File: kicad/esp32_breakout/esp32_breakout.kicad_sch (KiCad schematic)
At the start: 26 parts, among them J1 JST B5B-PH-K-S, J10 JST B6B-PH-K-S, J2 JST B5B-PH-K-S, J3 JST B7B-PH-K-S, J4 XT30U-M, J5 HDR F 2.54MM VERT, J6 HDR F 2.54MM 5-pin VERT, J9 JST B6B-PH-K-S, SW1 SS12D10, U1 ESP32 DEV KIT Module 30-pin, U2 LM2596 Module

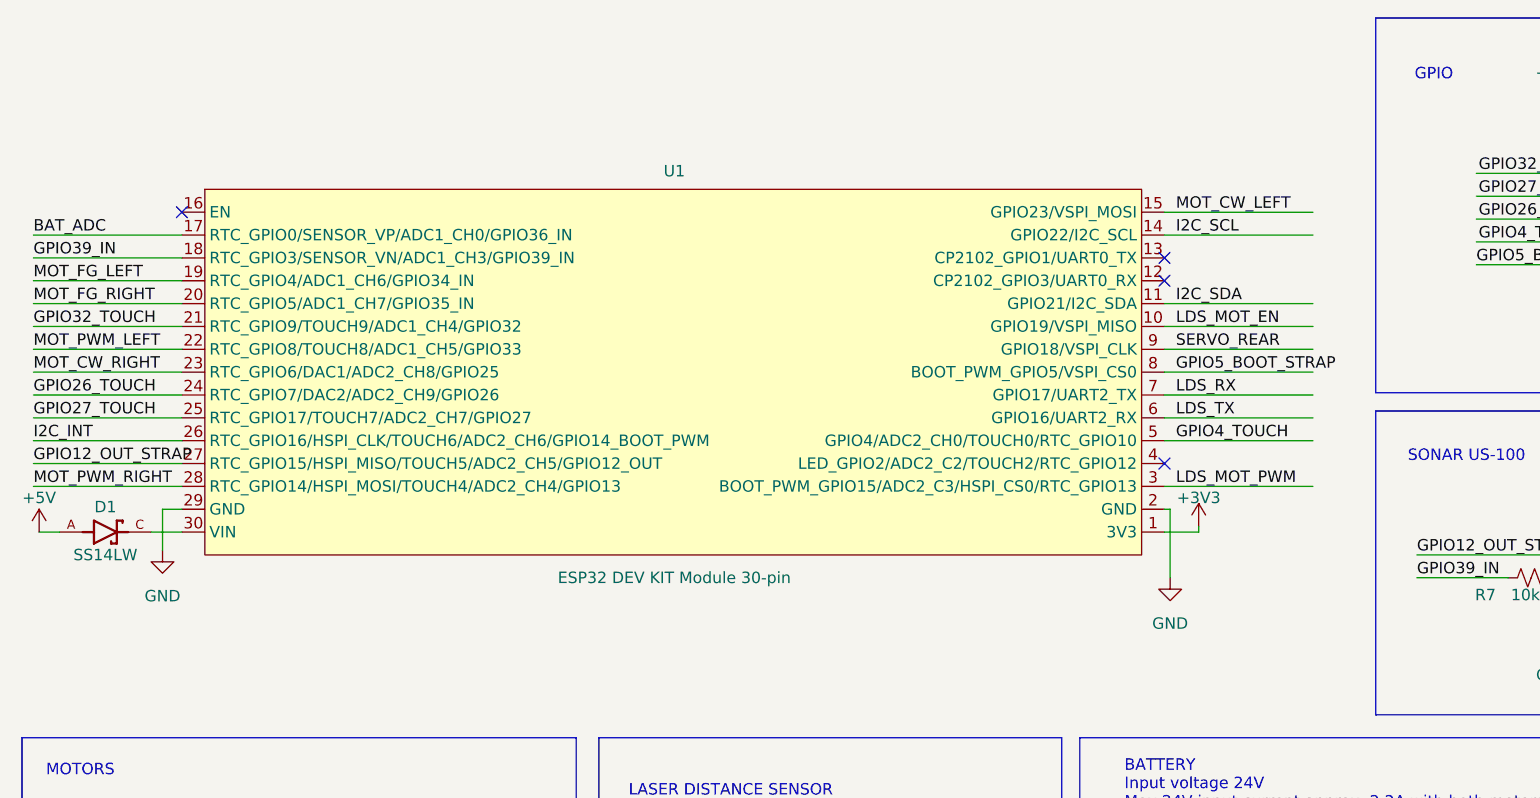
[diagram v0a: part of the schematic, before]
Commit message: Pico head breakout layout start
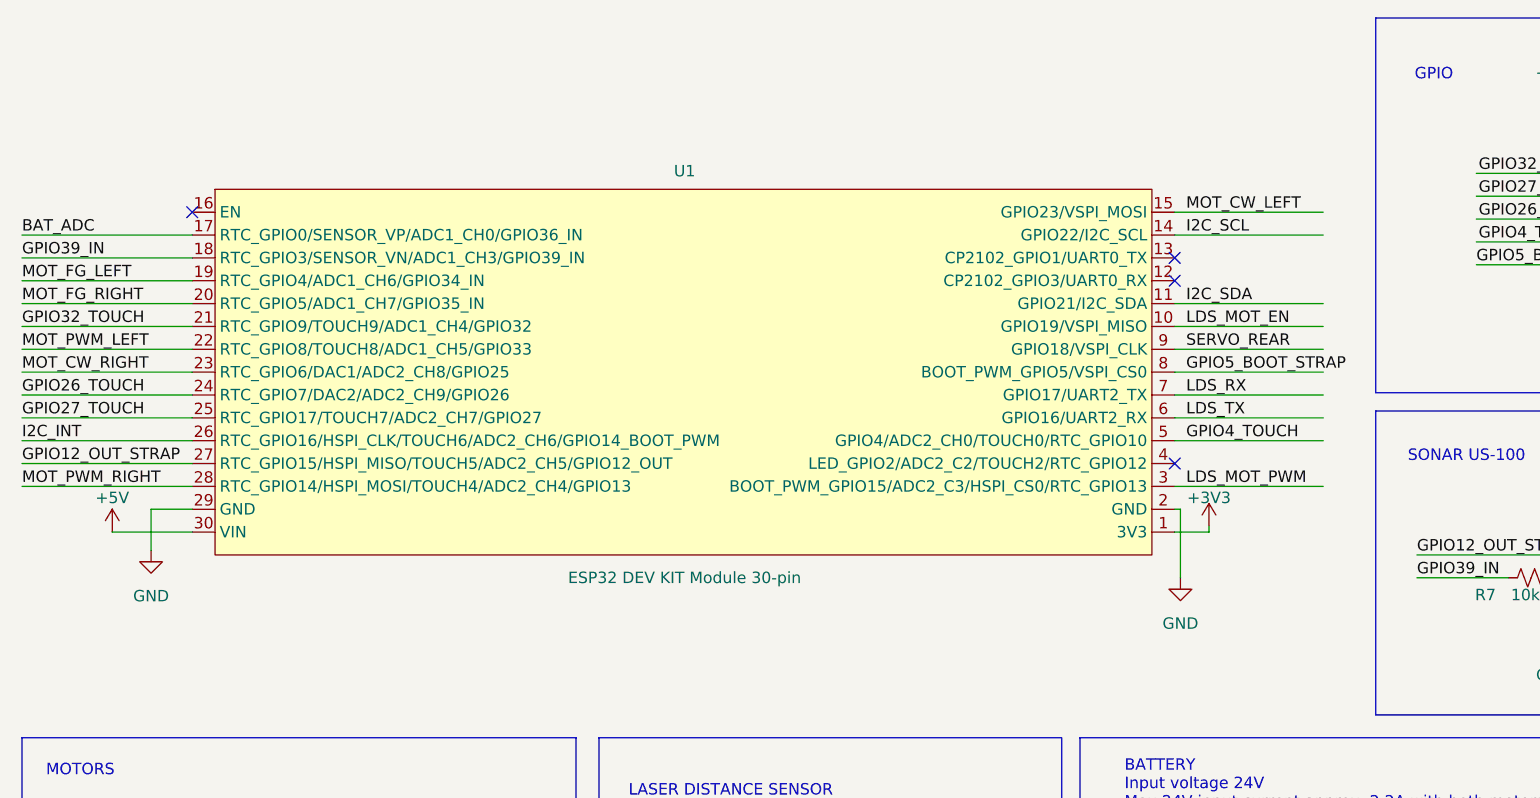
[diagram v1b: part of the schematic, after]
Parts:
- removed D1: SS14LW, SS14LW:DIO_SS14LW, symbol Makerspet:SS14LW
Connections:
- net +5V: now also U1.30 (VIN)
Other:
- moved on the sheet: U1

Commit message: ESP32 breakout v1.0
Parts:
- added D1: FS26, Diode_SMD:D_SOD-123F, symbol Device:D_Schottky
- J4: footprint Connector_AMASS:AMASS_XT30U-M_1x02_P5.0mm_Vertical -> Makerspet:AMASS_XT30U-F_1x02_P5.0mm_Vertical
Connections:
- net +5V: now also D1.2 (A); no longer U1.30 (VIN)
- new net: D1.1 (K), U1.30 (VIN)
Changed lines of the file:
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@@
   (title_block
     (title "Maker's Pet ESP32 Breakout")
-    (date "2023-12-12")
+    (date "2023-12-15")
     (rev "1.0.0")
     (company "Maker's Pet")
@@
     (stroke (width 0) (type default))
   )
+  (wire (pts (xy 27.94 72.39) (xy 33.528 72.39))
+    (stroke (width 0) (type default))
+  )
   (wire (pts (xy 143.383 69.85) (xy 143.383 77.47))
     (stroke (width 0) (type default))
@@
     (stroke (width 0) (type default))
   )
+  (wire (pts (xy 18.034 72.39) (xy 20.32 72.39))
+    (stroke (width 0) (type default))
+  )
   (wire (pts (xy 176.276 40.132) (xy 194.056 40.132))
     (stroke (width 0) (type default))
@@
   )
   (wire (pts (xy 146.05 150.114) (xy 162.56 150.114))
-    (stroke (width 0) (type default))
-  )
-  (wire (pts (xy 24.638 72.39) (xy 33.528 72.39))
     (stroke (width 0) (type default))
   )
@@
     )
   )
+  (symbol (lib_id "Device:D_Schottky") (at 24.13 72.39 0) (mirror y) (unit 1)
+    (in_bom yes) (on_board yes) (dnp no)
+    (property "Reference" "D1" (at 24.13 69.342 0)
+      (effects (font (size 1.27 1.27)))
+    )
+    (property "Value" "FS26" (at 23.876 75.438 0)
+      (effects (font (size 1.27 1.27)))
+    )
+    (property "Footprint" "Diode_SMD:D_SOD-123F" (at 24.13 72.39 0)
+      (effects (font (size 1.27 1.27)) hide)
+    )
+    (property "Datasheet" "https://www.digikey.com/en/products/detail/good-ark-semiconductor/FS26/18667798" (at 24.13 72.39 0)
+      (effects (font (size 1.27 1.27)) hide)
+    )
+    (pin "2")
+    (pin "1")
+    (instances
+      (project "esp32_breakout"
+        (path "/e24ae185-8f18-408c-aee8-f727519bade3"
+          (reference "D1") (unit 1)
+        )
+      )
+    )
+  )
   (symbol (lib_id "Switch:SW_SPDT") (at 189.23 127 0) (mirror y) (unit 1)
     (in_bom yes) (on_board yes) (dnp no)
@@
         (path "/e24ae185-8f18-408c-aee8-f727519bade3"
           (reference "H1") (unit 1)
-        )
-      )
-    )
-  )
-  (symbol (lib_id "power:+5V") (at 24.638 72.39 0) (unit 1)
-    (in_bom yes) (on_board yes) (dnp no) (fields_autoplaced)
-    (property "Reference" "#PWR02" (at 24.638 76.2 0)
-      (effects (font (size 1.27 1.27)) hide)
-    )
-    (property "Value" "+5V" (at 24.638 68.58 0)
-      (effects (font (size 1.27 1.27)))
-    )
-    (property "Footprint" "" (at 24.638 72.39 0)
-      (effects (font (size 1.27 1.27)) hide)
-    )
-    (property "Datasheet" "" (at 24.638 72.39 0)
-      (effects (font (size 1.27 1.27)) hide)
-    )
-    (pin "1")
-    (instances
-      (project "esp32_breakout"
-        (path "/e24ae185-8f18-408c-aee8-f727519bade3"
-          (reference "#PWR02") (unit 1)
         )
       )
@@
     )
   )
+  (symbol (lib_id "power:+5V") (at 18.034 72.39 0) (unit 1)
+    (in_bom yes) (on_board yes) (dnp no) (fields_autoplaced)
+    (property "Reference" "#PWR02" (at 18.034 76.2 0)
+      (effects (font (size 1.27 1.27)) hide)
+    )
+    (property "Value" "+5V" (at 18.034 68.58 0)
+      (effects (font (size 1.27 1.27)))
+    )
+    (property "Footprint" "" (at 18.034 72.39 0)
+      (effects (font (size 1.27 1.27)) hide)
+    )
+    (property "Datasheet" "" (at 18.034 72.39 0)
+      (effects (font (size 1.27 1.27)) hide)
+    )
+    (pin "1")
+    (instances
+      (project "esp32_breakout"
+        (path "/e24ae185-8f18-408c-aee8-f727519bade3"
+          (reference "#PWR02") (unit 1)
+        )
+      )
+    )
+  )
   (symbol (lib_id "Device:D_Schottky") (at 177.546 124.46 0) (mirror y) (unit 1)
     (in_bom yes) (on_board yes) (dnp no) (fields_autoplaced)
@@
       (effects (font (size 1.27 1.27)))
     )
-    (property "Footprint" "Connector_AMASS:AMASS_XT30U-M_1x02_P5.0mm_Vertical" (at 147.066 119.38 0)
-      (effects (font (size 1.27 1.27)) hide)
-    )
+    (property "Footprint" "Makerspet:AMASS_XT30U-F_1x02_P5.0mm_Vertical" (at 147.066 119.38 0)
+      (effects (font (size 1.27 1.27)) hide)
+    )

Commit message: Socket header
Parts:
- J6: footprint Connector_PinHeader_2.54mm:PinHeader_1x05_P2.54mm_Vertical -> Connector_PinSocket_2.54mm:PinSocket_1x05_P2.54mm_Vertical
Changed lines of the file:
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@@
       (effects (font (size 1.27 1.27)) (justify left))
     )
-    (property "Footprint" "Connector_PinHeader_2.54mm:PinHeader_1x05_P2.54mm_Vertical" (at 192.532 77.47 0)
+    (property "Footprint" "Connector_PinSocket_2.54mm:PinSocket_1x05_P2.54mm_Vertical" (at 192.532 77.47 0)
       (effects (font (size 1.27 1.27)) hide)
     )

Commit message: ESP32 board v1.1
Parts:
- added D3: FS26, Diode_SMD:D_SOD-123F, symbol Device:D_Schottky
- added Q1: AS2302, Package_TO_SOT_SMD:SOT-23, symbol Transistor_FET:BSS123
- added R5, R6: 10k, Resistor_SMD:R_0603_1608Metric, symbol Device:R_Small_US
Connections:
- net +5V: now also D3.1 (K)
- net GND: now also Q1.2 (S)
- net LDS_MOT_PWM: now also R5.2
- net LDS_TX: now also R6.1; no longer J3.2 (Pin_2)
- net LDS_MOT-: now reaches J3.6 (Pin_6)
- net LDS_MOT-: now also D3.2 (A), Q1.3 (D)
- new net: J3.2 (Pin_2), R6.2
- new net: Q1.1 (G), R5.1
- no-connect marks 6 -> 5

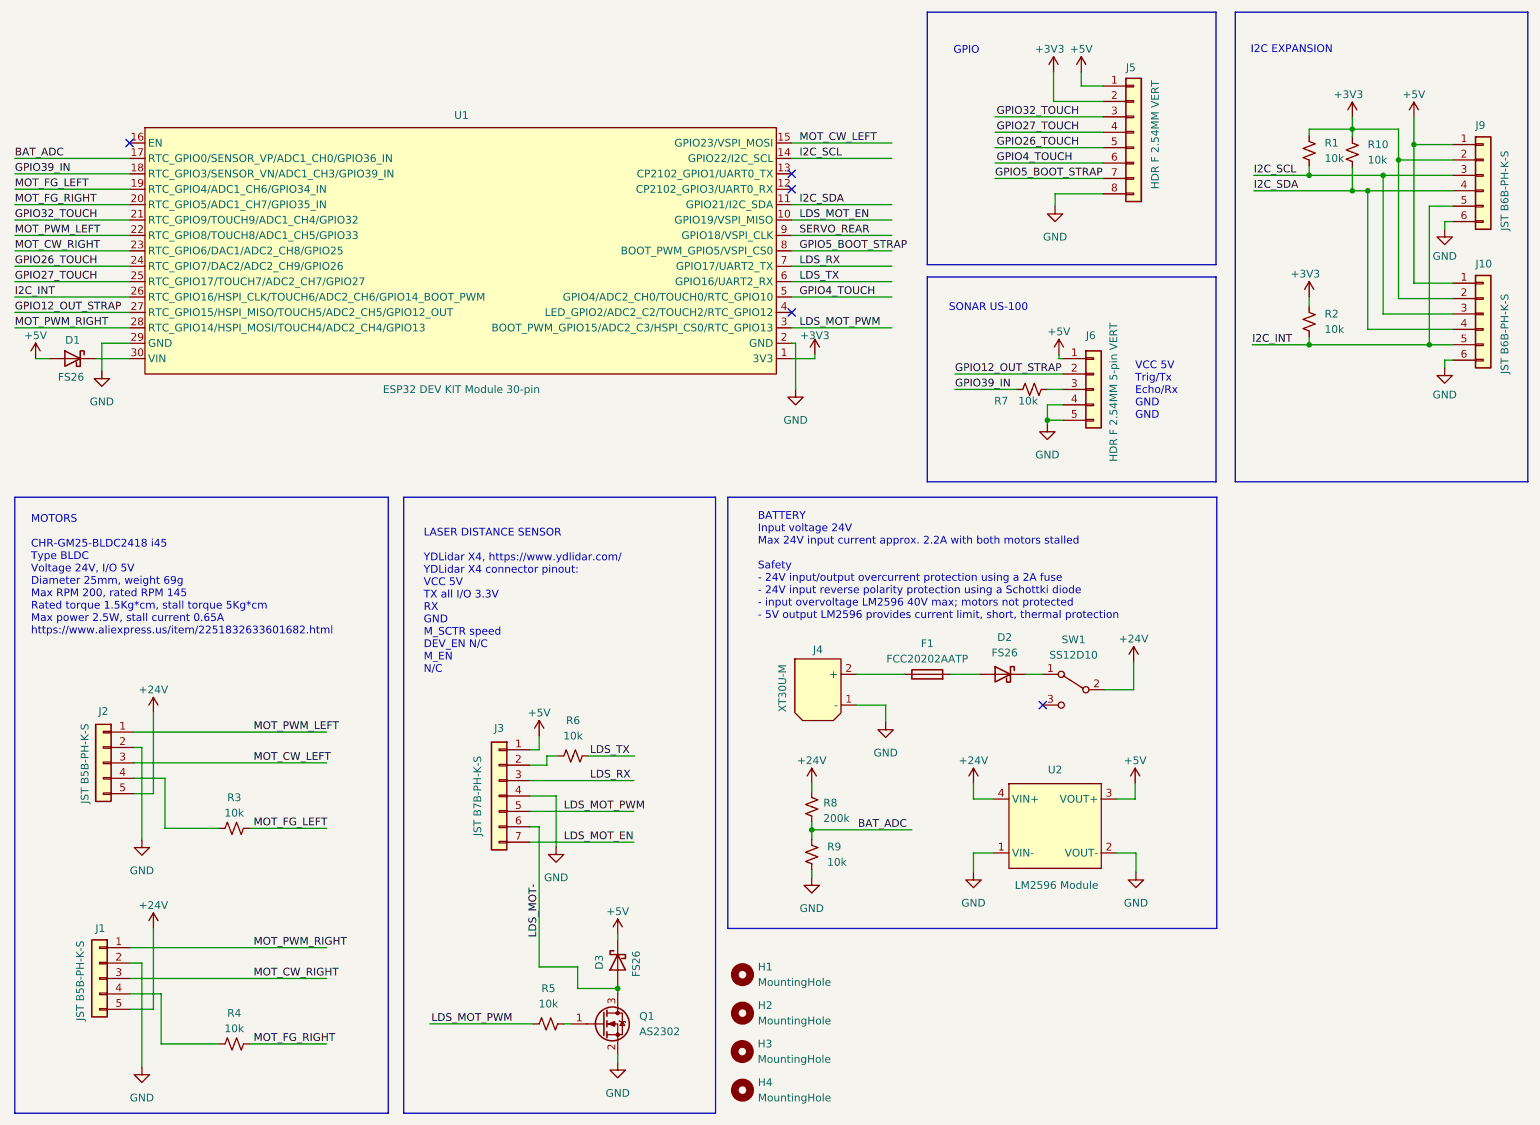
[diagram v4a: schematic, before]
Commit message: Reverted ESP32 PCB to v1
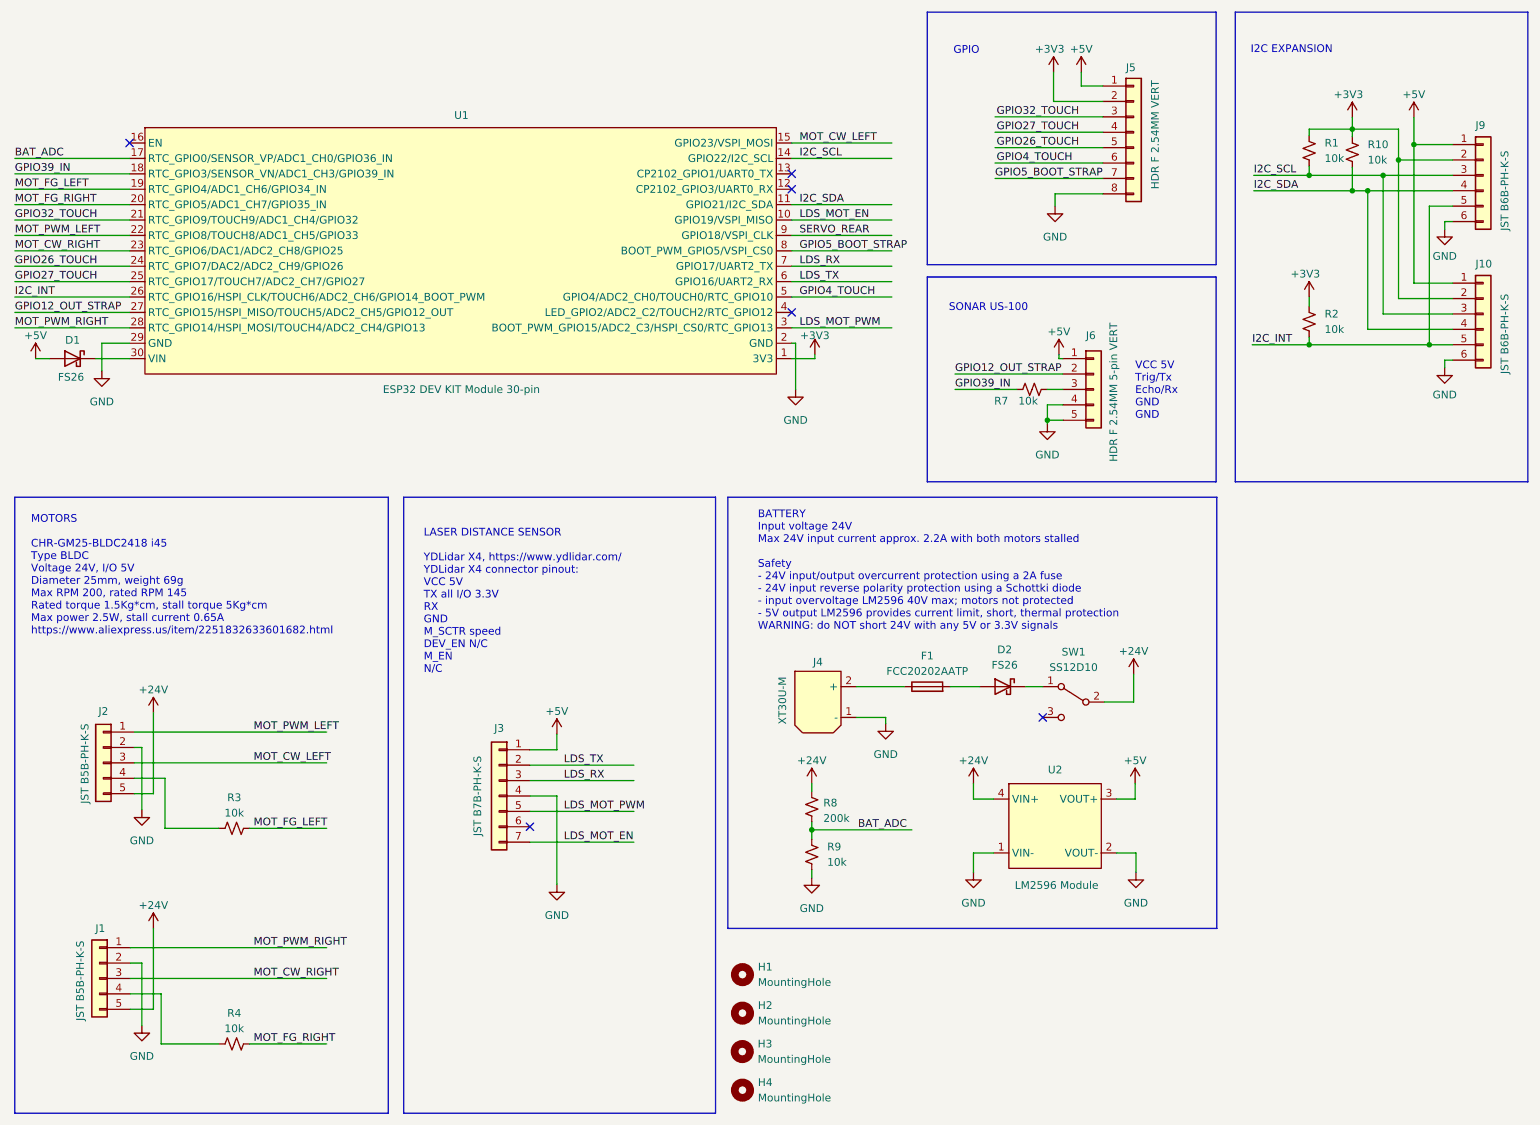
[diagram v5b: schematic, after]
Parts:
- removed D3: FS26, Diode_SMD:D_SOD-123F, symbol Device:D_Schottky
- removed Q1: AS2302, Package_TO_SOT_SMD:SOT-23, symbol Transistor_FET:BSS123
- removed R5, R6: 10k, Resistor_SMD:R_0603_1608Metric, symbol Device:R_Small_US
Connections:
- net LDS_TX: now also J3.2 (Pin_2)
- net LDS_MOT-: no longer names the net of J3.6 (Pin_6)
- no-connect marks 5 -> 6
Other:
- note added: "BATTERY Input voltage 24V Max 24V input current approx. 2.2A with both motors stalled Safety - 24V input/output overcurrent protection using a 2A fuse - 24V input reverse polarity protection using a Schottki diode - input overvoltage LM2596 40V max; motors not protected - 5V output LM2596 provides current limit, short, thermal protection WARNING: do NOT short 24V with any 5V or 3.3V signals"
- note removed: "BATTERY Input voltage 24V Max 24V input current approx. 2.2A with both motors stalled Safety - 24V input/output overcurrent protection using a 2A fuse - 24V input reverse polarity protection using a Schottki diode - input overvoltage LM2596 40V max; motors not protected - 5V output LM2596 provides current limit, short, thermal protection"
- moved on the sheet: D2, F1, J4, SW1

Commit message: Footprint fix
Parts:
- J5: footprint Connector_PinHeader_2.54mm:PinHeader_1x08_P2.54mm_Vertical -> Connector_PinSocket_2.54mm:PinSocket_1x08_P2.54mm_Vertical
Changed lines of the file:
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@@
   (title_block
     (title "Maker's Pet ESP32 Breakout")
-    (date "2023-12-15")
-    (rev "1.0.0")
+    (date "2023-12-24")
+    (rev "1.0.1")
     (company "Maker's Pet")
     (comment 1 "makerspet.com")
@@
       (effects (font (size 1.27 1.27)) (justify left))
     )
-    (property "Footprint" "Connector_PinHeader_2.54mm:PinHeader_1x08_P2.54mm_Vertical" (at 199.136 35.052 0)
-      (effects (font (size 1.27 1.27)) hide)
-    )
+    (property "Footprint" "Connector_PinSocket_2.54mm:PinSocket_1x08_P2.54mm_Vertical" (at 199.136 35.052 0)
+      (effects (font (size 1.27 1.27)) hide)
+    )
